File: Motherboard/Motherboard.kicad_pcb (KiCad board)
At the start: 4 copper layers, 246.4 x 175.3 mm, 52 parts, among them J1 40-pin IDE Connector, J3 Bus_ISA_8bit, J4 ATX-24, J5 USB_B, J6 ATF15XX_JTAG_ISP, J7 Bus_ISA_8bit, J8 65SIB_Connector, SW1 SW_Push, SW2 SW_SPST, U1 AS6C8008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

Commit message: 475 unrouted traces...
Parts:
- moved JP1 43.0 mm to (240.8, 158.0), turned to 180 degrees
- moved U11 32.1 mm to (131.7, 169.8)
- moved U2 8.60 mm to (137.7, 201.2)
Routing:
- net GND: track 756.4 -> 828.1 mm
- net ~{RESET}: track 75.0 -> 13.6 mm
- net +5V: track 282.5 -> 322.6 mm, vias 0 -> 5
- net Net-(U3-X1/CLK): track 0.00 -> 7.62 mm

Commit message: 472 unrouted traces...
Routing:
- net +12V: track 38.4 -> 229.5 mm, vias 0 -> 3
- net GND: track 828.1 -> 854.5 mm, vias 4 -> 3
- net +5V: track 322.6 -> 348.0 mm, vias 5 -> 6
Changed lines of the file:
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@@
   (segment (start 237.2614 75.1332) (end 237.2614 67.0056) (width 0.25) (layer "F.Cu") (net 1))
   (segment (start 223.2406 83.1342) (end 223.2152 83.1342) (width 0.25) (layer "F.Cu") (net 2))
-  (segment (start 223.266 107.8992) (end 223.1644 107.8992) (width 0.25) (layer "F.Cu") (net 2))
-  (segment (start 223.2406 107.9246) (end 223.266 107.8992) (width 0.25) (layer "F.Cu") (net 2))
-  (segment (start 223.1644 107.8992) (end 223.1644 108.0008) (width 0.25) (layer "F.Cu") (net 2))
-  (segment (start 223.2152 107.95) (end 223.2406 107.9754) (width 0.25) (layer "F.Cu") (net 2))
   (segment (start 223.266 83.185) (end 223.2406 83.1596) (width 0.25) (layer "F.Cu") (net 2))
   (segment (start 240.03 86.1175) (end 240.03 80.137) (width 0.25) (layer "F.Cu") (net 2))
   (segment (start 240.03 80.137) (end 240.0554 80.1116) (width 0.25) (layer "F.Cu") (net 2))
-  (segment (start 223.2406 107.9754) (end 224.8662 107.9754) (width 0.25) (layer "F.Cu") (net 2))
   (segment (start 223.2152 83.1342) (end 223.2406 83.1596) (width 0.25) (layer "F.Cu") (net 2))
   (segment (start 223.2406 83.1596) (end 223.2406 83.1342) (width 0.25) (layer "F.Cu") (net 2))
   (segment (start 225.63 83.185) (end 225.6028 77.6732) (width 0.25) (layer "F.Cu") (net 2))
   (segment (start 225.63 83.185) (end 223.266 83.185) (width 0.25) (layer "F.Cu") (net 2))
-  (segment (start 223.1644 108.0008) (end 223.2152 107.95) (width 0.25) (layer "F.Cu") (net 2))
   (segment (start 88.4174 180.1876) (end 100.3046 180.1876) (width 0.25) (layer "F.Cu") (net 2))
   (segment (start 100.3046 180.1876) (end 102.23 178.2622) (width 0.25) (layer "F.Cu") (net 2))
   (via (at 223.2406 83.1342) (size 0.8) (drill 0.4) (layers "F.Cu" "B.Cu") (net 2))
   (via (at 240.0554 80.1116) (size 0.8) (drill 0.4) (layers "F.Cu" "B.Cu") (net 2))
-  (via (at 223.1644 107.8992) (size 0.8) (drill 0.4) (layers "F.Cu" "B.Cu") (net 2))
   (via (at 225.6028 77.6732) (size 0.8) (drill 0.4) (layers "F.Cu" "B.Cu") (net 2))
-  (segment (start 223.2406 83.1342) (end 223.2406 107.823) (width 0.25) (layer "In1.Cu") (net 2))
-  (segment (start 223.2406 107.823) (end 223.1644 107.8992) (width 0.25) (layer "In1.Cu") (net 2))
   (segment (start 235.5166 65.8254) (end 235.5166 79.966) (width 0.25) (layer "B.Cu") (net 2))
   (segment (start 227.9542 80.0246) (end 231.394 80.0246) (width 0.25) (layer "B.Cu") (net 2))
@@
   (segment (start 213.36 157.48) (end 214.3962 158.5162) (width 0.25) (layer "B.Cu") (net 2))
   (segment (start 88.4174 197.9676) (end 87.122 199.263) (width 0.25) (layer "B.Cu") (net 2))
+  (segment (start 222.4838 133.5838) (end 222.4838 106.9288) (width 0.25) (layer "B.Cu") (net 2))
   (segment (start 155.18 82.435) (end 153.00548 80.26048) (width 0.25) (layer "B.Cu") (net 2))
   (segment (start 90.02 96.52) (end 101.6 96.52) (width 0.25) (layer "B.Cu") (net 2))
@@
   (segment (start 225.298 77.3684) (end 225.6028 77.6732) (width 0.25) (layer "B.Cu") (net 2))
   (segment (start 91.0336 87.3506) (end 97.1804 87.3506) (width 0.25) (layer "B.Cu") (net 2))
+  (segment (start 223.2406 106.172) (end 223.2406 106.3498) (width 0.25) (layer "B.Cu") (net 2))
   (segment (start 167.68 101.1536) (end 165.227 101.1536) (width 0.25) (layer "B.Cu") (net 2))
   (segment (start 232.2764 135.7564) (end 231.14 134.62) (width 0.25) (layer "B.Cu") (net 2))
@@
   (segment (start 212.3238 156.4438) (end 213.36 157.48) (width 0.25) (layer "B.Cu") (net 2))
   (segment (start 200.66 157.48) (end 201.6962 156.4438) (width 0.25) (layer "B.Cu") (net 2))
+  (segment (start 223.2406 106.3498) (end 224.8662 107.9754) (width 0.25) (layer "B.Cu") (net 2))
   (segment (start 209.7838 131.0438) (end 219.9438 131.0438) (width 0.25) (layer "B.Cu") (net 2))
   (segment (start 87.2424 196.7926) (end 88.4174 197.9676) (width 0.25) (layer "B.Cu") (net 2))
@@
   (segment (start 232.0216 214.5866) (end 214.485 214.5866) (width 0.25) (layer "B.Cu") (net 2))
   (segment (start 87.122 201.803) (end 85.8774 203.0476) (width 0.25) (layer "B.Cu") (net 2))
+  (segment (start 222.4838 106.9288) (end 223.2406 106.172) (width 0.25) (layer "B.Cu") (net 2))
   (segment (start 110.2614 131.2672) (end 110.236 131.2926) (width 0.25) (layer "B.Cu") (net 2))
   (segment (start 275.463 134.3914) (end 278.4856 137.414) (width 0.25) (layer "B.Cu") (net 2))
@@
   (segment (start 153.00548 80.26048) (end 136.35452 80.26048) (width 0.25) (layer "B.Cu") (net 2))
   (segment (start 106.426 120.8532) (end 106.4768 120.904) (width 0.25) (layer "B.Cu") (net 2))
+  (segment (start 223.2406 83.1342) (end 223.2406 106.172) (width 0.25) (layer "B.Cu") (net 2))
   (segment (start 173.6852 89.5858) (end 196.6164 89.5858) (width 0.25) (layer "B.Cu") (net 2))
   (segment (start 105.7148 120.904) (end 104.8512 120.0404) (width 0.25) (layer "B.Cu") (net 2))
@@
   (segment (start 228.346 82.5246) (end 231.394 82.5246) (width 0.25) (layer "F.Cu") (net 3))
   (segment (start 167.6654 93.7406) (end 167.6654 88.9254) (width 0.25) (layer "In2.Cu") (net 4))
+  (via (at 82.423 72.517) (size 0.8) (drill 0.4) (layers "F.Cu" "B.Cu") (net 5))
+  (via (at 82.423 187.706) (size 0.8) (drill 0.4) (layers "F.Cu" "B.Cu") (net 5))
+  (via (at 146.939 72.517) (size 0.8) (drill 0.4) (layers "F.Cu" "B.Cu") (net 5))
+  (segment (start 82.423 72.517) (end 82.423 187.706) (width 0.25) (layer "In1.Cu") (net 5))
+  (segment (start 146.78 76.935) (end 146.78 72.676) (width 0.25) (layer "In1.Cu") (net 5))
+  (segment (start 146.78 72.676) (end 146.939 72.517) (width 0.25) (layer "In1.Cu") (net 5))
+  (segment (start 146.939 72.517) (end 82.423 72.517) (width 0.25) (layer "In2.Cu") (net 5))
   (segment (start 150.98 79.9314) (end 150.9776 79.9338) (width 0.25) (layer "In2.Cu") (net 5))
   (segment (start 165.2016 80.01) (end 165.1 80.1116) (width 0.25) (layer "In2.Cu") (net 5))
   (segment (start 165.1 88.9) (end 165.1 98.5266) (width 0.25) (layer "In2.Cu") (net 5))
+  (segment (start 82.423 187.706) (end 83.4964 186.6326) (width 0.25) (layer "In2.Cu") (net 5))
   (segment (start 150.98 76.935) (end 150.98 79.9314) (width 0.25) (layer "In2.Cu") (net 5))
+  (segment (start 87.2424 186.6326) (end 88.4174 187.8076) (width 0.25) (layer "In2.Cu") (net 5))
+  (segment (start 83.4964 186.6326) (end 87.2424 186.6326) (width 0.25) (layer "In2.Cu") (net 5))
   (segment (start 150.9776 79.9338) (end 165.1254 79.9338) (width 0.25) (layer "In2.Cu") (net 5))
   (segment (start 165.1254 79.9338) (end 165.2016 80.01) (width 0.25) (layer "In2.Cu") (net 5))
@@
   (via (at 257.302 93.98) (size 0.8) (drill 0.4) (layers "F.Cu" "B.Cu") (net 29))
   (via (at 169.3746 99.7786) (size 0.8) (drill 0.4) (layers "F.Cu" "B.Cu") (net 29))
+  (via (at 213.36 104.14) (size 0.8) (drill 0.4) (layers "F.Cu" "B.Cu") (net 29))
   (via (at 257.302 82.804) (size 0.8) (drill 0.4) (layers "F.Cu" "B.Cu") (net 29))
   (via (at 237.49 104.14) (size 0.8) (drill 0.4) (layers "F.Cu" "B.Cu") (net 29))
@@
   (segment (start 169.2248 99.9284) (end 169.2248 127.1574) (width 0.25) (layer "In1.Cu") (net 29))
   (segment (start 209.6262 104.0638) (end 209.6262 100.3554) (width 0.25) (layer "In1.Cu") (net 29))
+  (segment (start 213.36 129.54) (end 213.36 104.14) (width 0.25) (layer "In1.Cu") (net 29))
   (segment (start 257.302 93.98) (end 257.302 82.804) (width 0.25) (layer "In1.Cu") (net 29))
   (segment (start 169.3746 99.7786) (end 169.2248 99.9284) (width 0.25) (layer "In1.Cu") (net 29))
@@
   (segment (start 169.418 99.822) (end 169.3746 99.7786) (width 0.25) (layer "In2.Cu") (net 29))
   (segment (start 121.92 113.411) (end 121.92 105.75) (width 0.25) (layer "In2.Cu") (net 29))
+  (segment (start 213.36 104.14) (end 209.55 104.14) (width 0.25) (layer "In2.Cu") (net 29))
   (segment (start 126.4158 128.8034) (end 126.492 128.7272) (width 0.25) (layer "In2.Cu") (net 29))
   (segment (start 88.695 106.165518) (end 88.695 95.9122) (width 0.25) (layer "In2.Cu") (net 29))
@@
   (segment (start 257.302 82.804) (end 255.397 82.804) (width 0.25) (layer "In2.Cu") (net 29))
   (segment (start 130.1242 128.7272) (end 136.7182 128.7272) (width 0.25) (layer "In2.Cu") (net 29))
-  (segment (start 237.49 104.14) (end 209.55 104.14) (width 0.25) (layer "In2.Cu") (net 29))
   (segment (start 89.6112 112.4204) (end 89.6112 107.081718) (width 0.25) (layer "In2.Cu") (net 29))
   (segment (start 140.7922 79.5274) (end 142.58 81.3152) (width 0.25) (layer "In2.Cu") (net 29))
+  (segment (start 237.49 104.14) (end 213.36 104.14) (width 0.25) (layer "In2.Cu") (net 29))
   (segment (start 123.255 78.61) (end 121.58 76.935) (width 0.25) (layer "In2.Cu") (net 29))
   (segment (start 149.0472 99.314) (end 154.9654 99.314) (width 0.25) (layer "In2.Cu") (net 29))

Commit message: 443 unrouted traces...
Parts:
- moved J1 0.48 mm to (312.7, 157.7)
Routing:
- net +5V: track 348.0 -> 575.5 mm
- net GND: track 854.5 -> 1005.5 mm
- net IDE_D7: track 0.00 -> 19.0 mm
- net IDE_D6: track 0.00 -> 19.0 mm
- net IDE_D5: track 0.00 -> 19.0 mm
- net IDE_D4: track 0.00 -> 19.0 mm
- net IDE_D3: track 0.00 -> 19.0 mm

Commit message: 354 unrouted traces...
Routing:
- net A14: track 0.00 -> 62.6 mm
- net A12: track 0.00 -> 62.6 mm
- net A11: track 0.00 -> 62.4 mm
- net A10: track 0.00 -> 62.4 mm
- net A17: track 0.00 -> 62.4 mm
- net A7: track 0.00 -> 62.3 mm
- net A8: track 0.00 -> 62.2 mm
- net A5: track 0.00 -> 62.1 mm
- net D7: track 0.00 -> 62.1 mm
- net A13: track 0.00 -> 62.1 mm
- net D5: track 0.00 -> 62.1 mm
- net A9: track 0.00 -> 62.1 mm
- net D6: track 0.00 -> 62.1 mm
- net A6: track 0.00 -> 62.1 mm
- net A18: track 0.00 -> 62.1 mm
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
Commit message: 350 unrouted traces...
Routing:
- net +5V: track 575.5 -> 671.1 mm, vias 6 -> 8
- net ~{RESET}: track 13.6 -> 84.9 mm, vias 0 -> 2
- net ~{IRQ}: track 17.4 -> 24.0 mm, vias 0 -> 1
- net +12V: track 229.3 -> 233.5 mm
- net ~{NMI}: track 30.5 -> 34.1 mm, vias 0 -> 1
- net RDY: track 9.65 -> 12.5 mm, vias 0 -> 1

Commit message: Fixed clock connections...
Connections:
- net NOT_PHI2 renamed NOT_CLK_STR
- U10 pad 83: CLK_STD -> CLK_STR
- U8 pad 37: CLK_STD -> CLK_STR
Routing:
- net CLK_STD: track 24.3 -> 0.00 mm
- net +5V: track 671.1 -> 669.2 mm
- net GND: track 1052.3 -> 1051.0 mm
- net Net-(U17-D3): track 8.20 -> 7.65 mm
- net Net-(D4-A): track 26.6 -> 26.1 mm

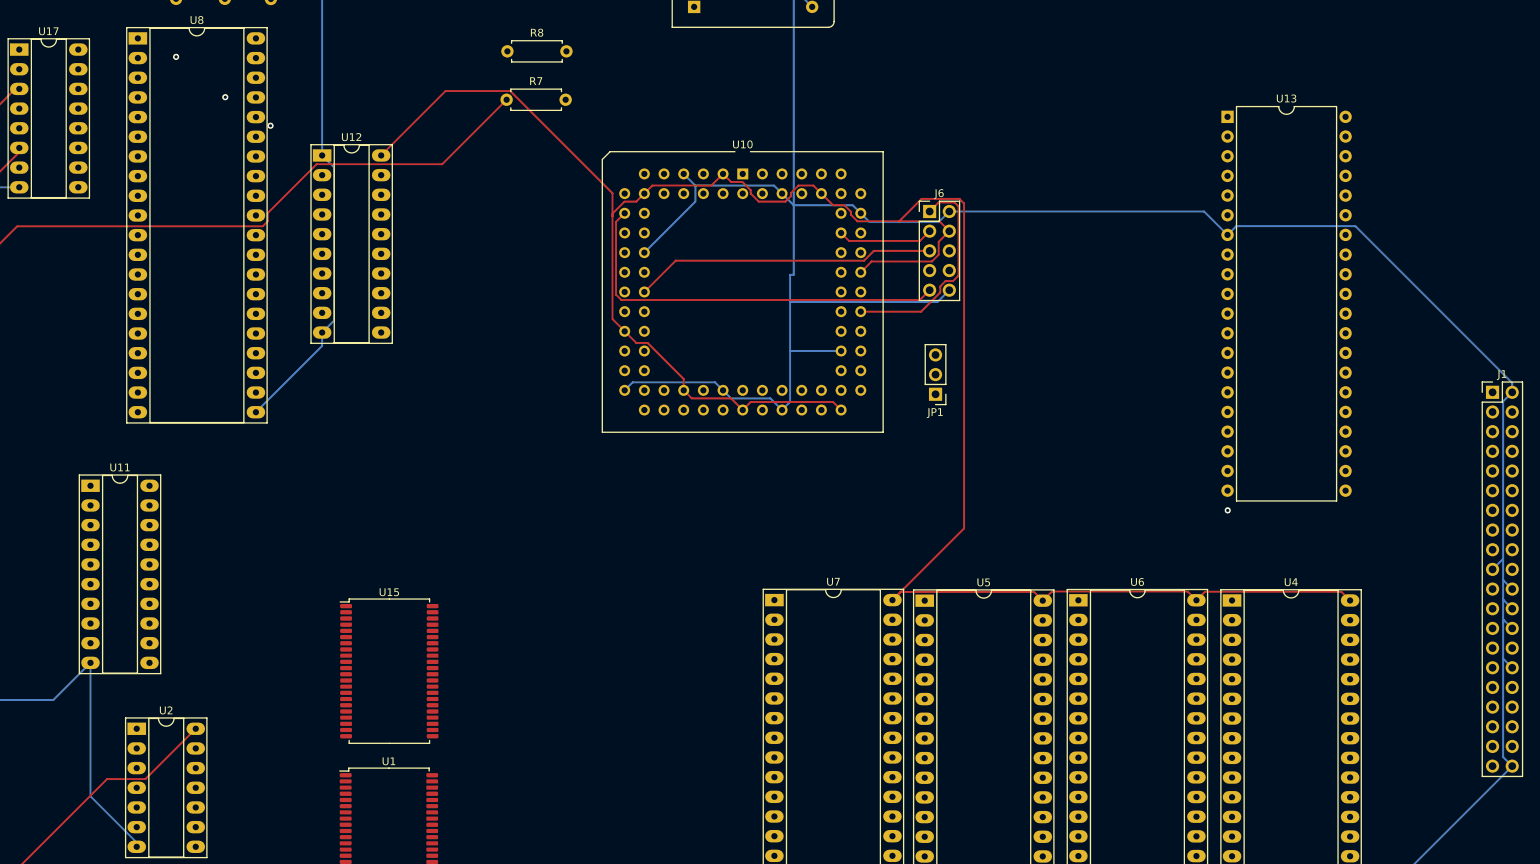
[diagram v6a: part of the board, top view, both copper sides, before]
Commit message: 340 unrouted traces...
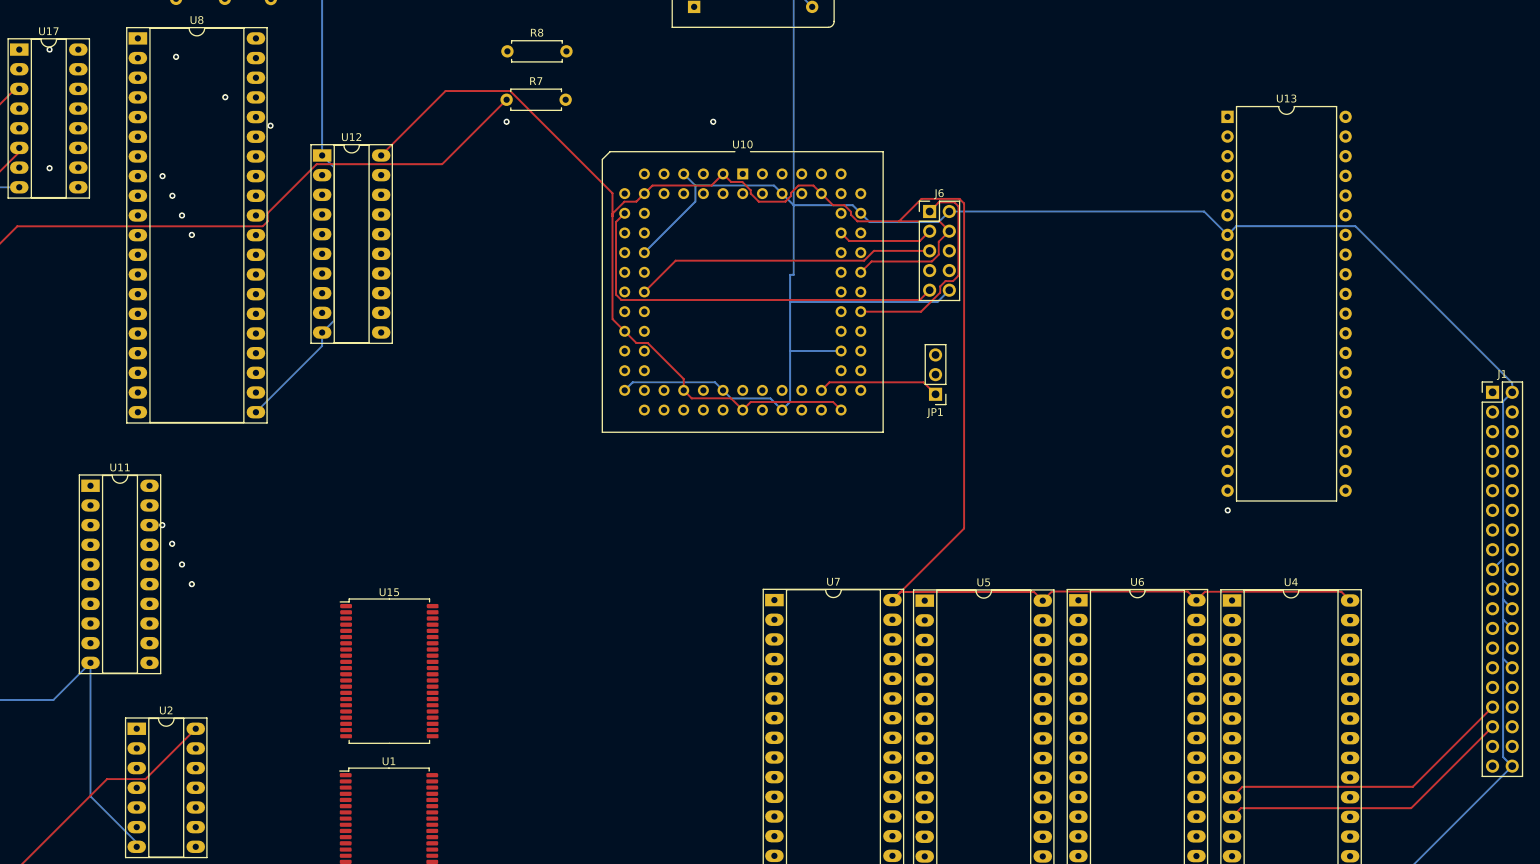
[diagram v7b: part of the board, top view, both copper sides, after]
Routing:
- net Net-(D3-A): track 4.55 -> 79.3 mm
- net Net-(D2-A): track 5.68 -> 80.1 mm
- net DA3: track 8.42 -> 67.4 mm, vias 0 -> 2
- net DA0: track 8.42 -> 67.4 mm, vias 0 -> 2
- net DA2: track 8.42 -> 67.4 mm, vias 0 -> 2
- net DA1: track 8.42 -> 67.3 mm, vias 0 -> 2
- net ~{HALT}: track 92.7 -> 132.2 mm, vias 0 -> 2
- net A1: track 61.9 -> 100.3 mm
- net A0: track 61.9 -> 100.3 mm
- net CLK_STR: track 0.00 -> 24.9 mm
- net ~{UART_IRQ}: track 0.00 -> 15.8 mm
- net DA5: track 8.34 -> 9.99 mm
- net +5V: track 669.2 -> 669.1 mm, vias 8 -> 10

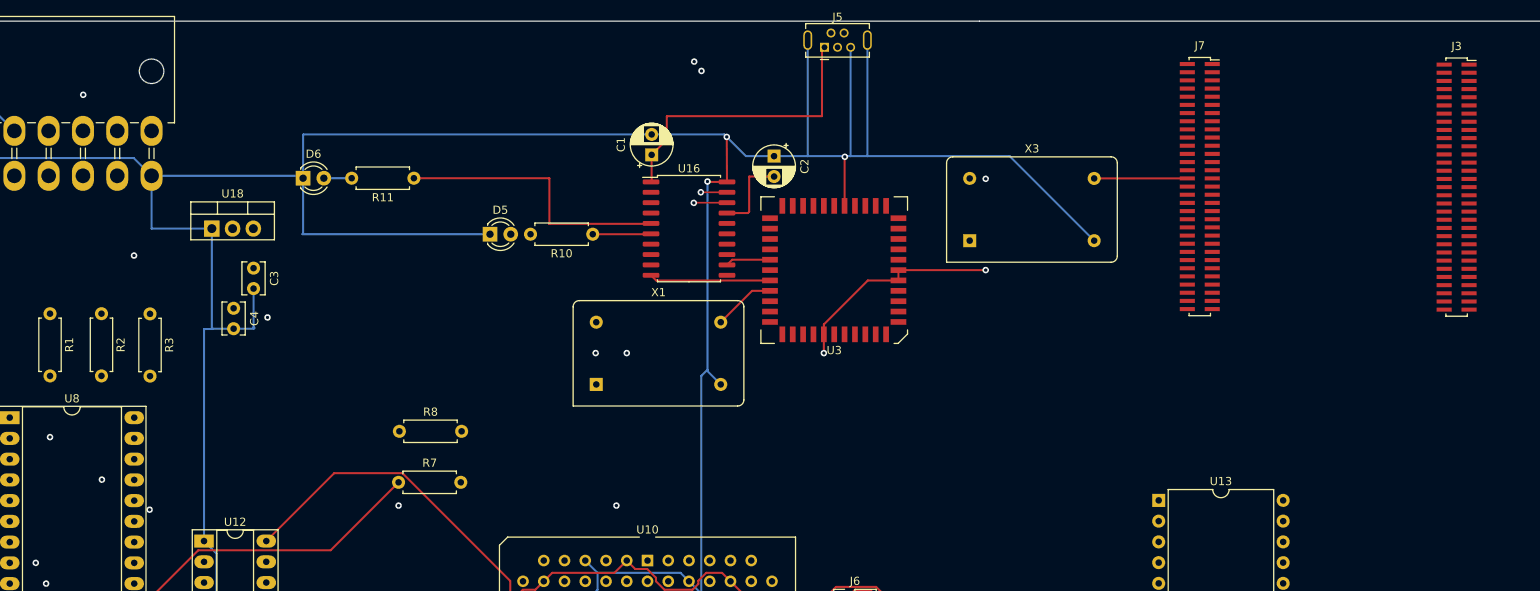
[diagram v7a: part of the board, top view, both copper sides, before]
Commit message: 334 unrouted traces...
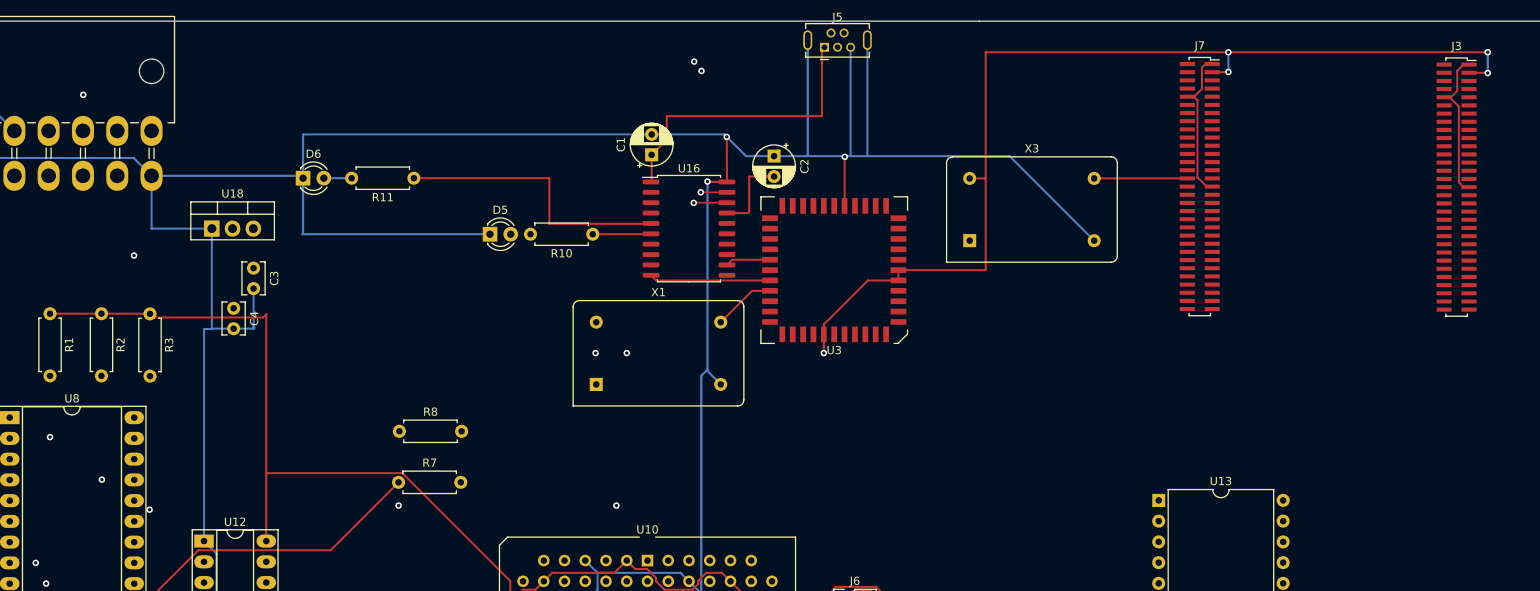
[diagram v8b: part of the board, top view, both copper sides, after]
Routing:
- net +5V: track 669.1 -> 752.4 mm, vias 10 -> 11
- net GND: track 1051.0 -> 1088.8 mm
